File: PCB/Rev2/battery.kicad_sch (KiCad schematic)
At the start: 11 parts, among them U2 TP4057, U3 TPS2116DRL, U4 TPS2116DRL

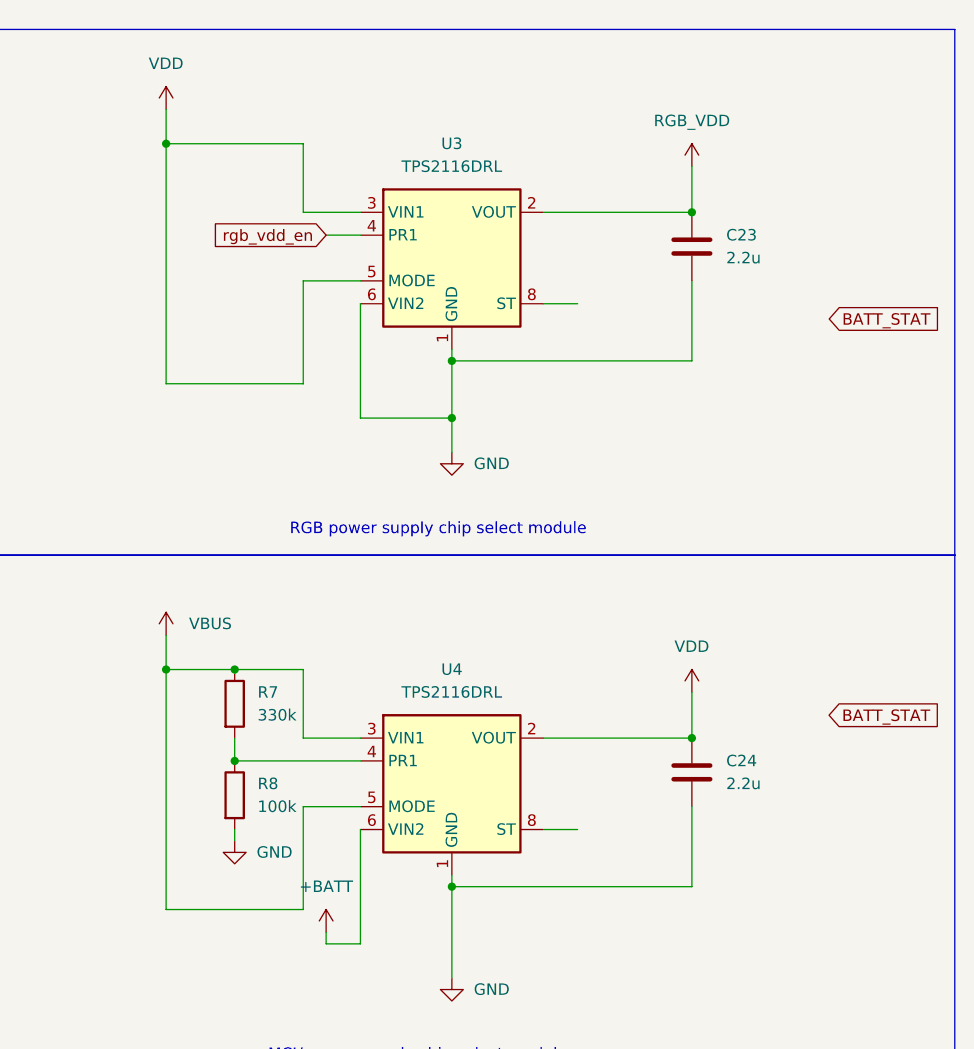
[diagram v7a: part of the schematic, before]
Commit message: Fix RGB_VDD
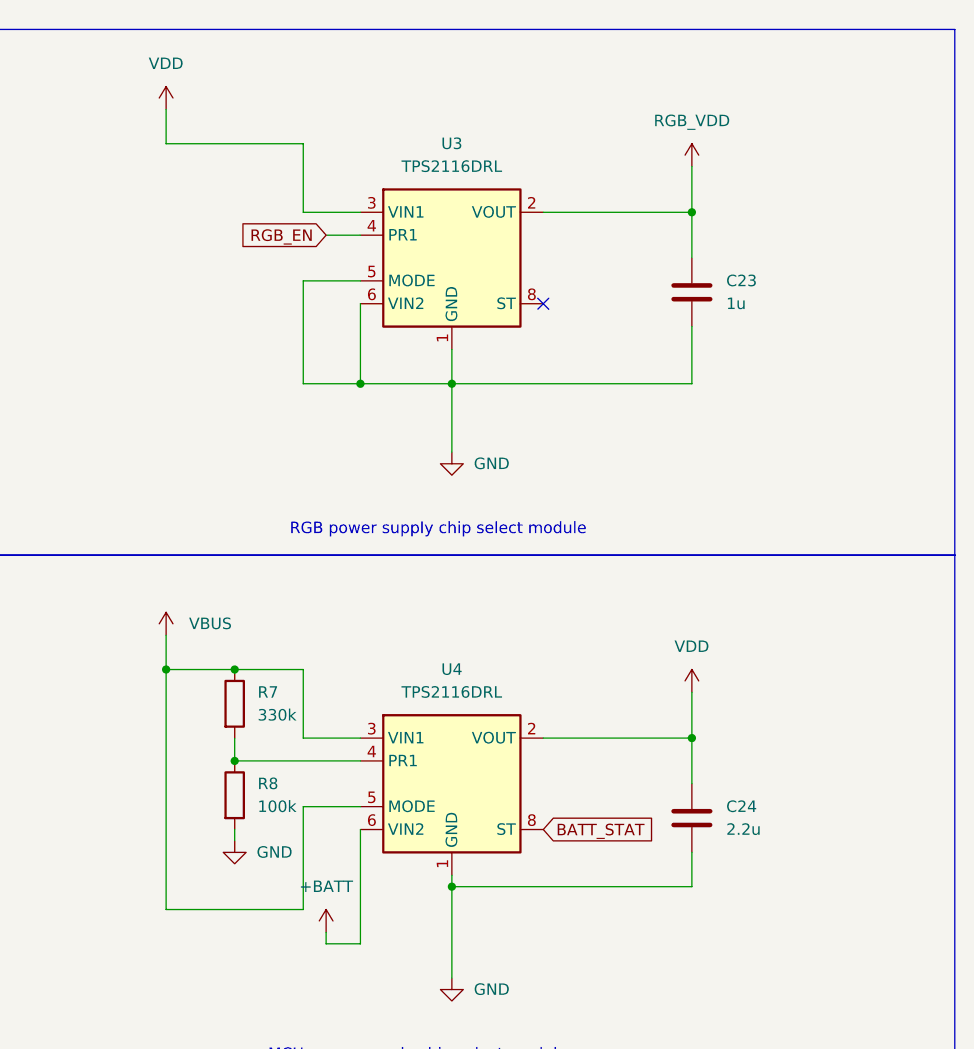
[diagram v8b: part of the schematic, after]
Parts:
- C23: value 2.2u -> 1u
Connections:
- net BATT_STAT: now also U4.8 (ST)
- net GND: now also U3.5 (MODE)
- net VDD: no longer U3.5 (MODE)
- net rgb_vdd_en renamed RGB_EN
- no-connect marks 2 -> 3
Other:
- moved on the sheet: C23
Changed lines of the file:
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@@
+	)
+	(junction
+		(at 171.45 52.07)
+		(diameter 0)
+		(color 0 0 0 0)
 	)
 	(junction
@@
 	)
 	(junction
+		(at 161.29 52.07)
+		(diameter 0)
+		(color 0 0 0 0)
+	)
+	(junction
 		(at 59.69 52.07)
 		(diameter 0)
@@
 	)
 	(junction
-		(at 171.45 55.88)
+		(at 95.25 36.83)
 		(diameter 0)
 		(color 0 0 0 0)
 	)
 	(junction
-		(at 95.25 36.83)
+		(at 198.12 91.44)
 		(diameter 0)
 		(color 0 0 0 0)
@@
 	)
 	(junction
-		(at 139.7 25.4)
-		(diameter 0)
-		(color 0 0 0 0)
-	)
-	(junction
-		(at 198.12 91.44)
-		(diameter 0)
-		(color 0 0 0 0)
-	)
-	(junction
-		(at 171.45 49.53)
-		(diameter 0)
-		(color 0 0 0 0)
-	)
-	(junction
 		(at 139.7 83.82)
 		(diameter 0)
@@
 	)
 	(no_connect
+		(at 181.61 43.18)
+	)
+	(no_connect
 		(at 49.53 46.99)
 	)
 	(wire
 		(pts
-			(xy 185.42 101.6) (xy 181.61 101.6)
+			(xy 198.12 52.07) (xy 198.12 45.72)
 		)
 		(stroke
@@
 	(wire
 		(pts
+			(xy 154.94 52.07) (xy 161.29 52.07)
+		)
+		(stroke
+			(width 0)
+			(type default)
+		)
+	)
+	(wire
+		(pts
 			(xy 171.45 107.95) (xy 198.12 107.95)
 		)
@@
 	(wire
 		(pts
-			(xy 171.45 55.88) (xy 171.45 59.69)
-		)
-		(stroke
-			(width 0)
-			(type default)
-		)
-	)
-	(wire
-		(pts
-			(xy 154.94 52.07) (xy 154.94 40.64)
-		)
-		(stroke
-			(width 0)
-			(type default)
-		)
-	)
-	(wire
-		(pts
 			(xy 139.7 110.49) (xy 154.94 110.49)
 		)
@@
 	(wire
 		(pts
-			(xy 139.7 52.07) (xy 154.94 52.07)
-		)
-		(stroke
-			(width 0)
-			(type default)
-		)
-	)
-	(wire
-		(pts
 			(xy 181.61 91.44) (xy 198.12 91.44)
 		)
@@
 	(wire
 		(pts
+			(xy 154.94 40.64) (xy 154.94 52.07)
+		)
+		(stroke
+			(width 0)
+			(type default)
+		)
+	)
+	(wire
+		(pts
 			(xy 198.12 86.36) (xy 198.12 91.44)
 		)
@@
 	(wire
 		(pts
-			(xy 171.45 49.53) (xy 171.45 55.88)
+			(xy 171.45 48.26) (xy 171.45 52.07)
+		)
+		(stroke
+			(width 0)
+			(type default)
+		)
+	)
+	(wire
+		(pts
+			(xy 171.45 52.07) (xy 171.45 59.69)
 		)
 		(stroke
@@
 	(wire
 		(pts
-			(xy 198.12 40.64) (xy 198.12 49.53)
+			(xy 171.45 52.07) (xy 198.12 52.07)
 		)
 		(stroke
@@
 	(wire
 		(pts
-			(xy 139.7 25.4) (xy 139.7 52.07)
-		)
-		(stroke
-			(width 0)
-			(type default)
-		)
-	)
-	(wire
-		(pts
-			(xy 171.45 48.26) (xy 171.45 49.53)
-		)
-		(stroke
-			(width 0)
-			(type default)
-		)
-	)
-	(wire
-		(pts
 			(xy 147.32 93.98) (xy 147.32 91.44)
 		)
@@
 	(wire
 		(pts
-			(xy 171.45 49.53) (xy 198.12 49.53)
+			(xy 198.12 104.14) (xy 198.12 107.95)
 		)
 		(stroke
@@
 	(wire
 		(pts
-			(xy 185.42 43.18) (xy 181.61 43.18)
-		)
-		(stroke
-			(width 0)
-			(type default)
-		)
-	)
-	(wire
-		(pts
 			(xy 95.25 36.83) (xy 95.25 39.37)
 		)
@@
 	(wire
 		(pts
-			(xy 198.12 99.06) (xy 198.12 107.95)
+			(xy 198.12 91.44) (xy 198.12 96.52)
+		)
+		(stroke
+			(width 0)
+			(type default)
+		)
+	)
+	(wire
+		(pts
+			(xy 198.12 38.1) (xy 198.12 33.02)
 		)
 		(stroke
@@
 	(wire
 		(pts
-			(xy 161.29 43.18) (xy 161.29 55.88)
-		)
-		(stroke
-			(width 0)
-			(type default)
-		)
-	)
-	(wire
-		(pts
-			(xy 161.29 55.88) (xy 171.45 55.88)
+			(xy 161.29 43.18) (xy 161.29 52.07)
+		)
+		(stroke
+			(width 0)
+			(type default)
+		)
+	)
+	(wire
+		(pts
+			(xy 161.29 52.07) (xy 171.45 52.07)
 		)
 		(stroke
@@
 		)
 	)
-	(global_label "rgb_vdd_en"
+	(global_label "RGB_EN"
 		(shape input)
 		(at 157.48 35.56 180)
@@
 		)
 		(property "Intersheetrefs" "${INTERSHEET_REFS}"
-			(at 143.9722 35.56 0)
+			(at 147.2377 35.56 0)
 			(effects
 				(font
@@
 	(global_label "BATT_STAT"
 		(shape input)
-		(at 213.3773 44.8722 0)
+		(at 181.61 101.6 0)
 		(fields_autoplaced yes)
 		(effects
@@
 		)
 		(property "Intersheetrefs" "${INTERSHEET_REFS}"
-			(at 225.8572 44.8722 0)
-			(effects
-				(font
-					(size 1.27 1.27)
-				)
-				(justify left)
-				(hide yes)
-			)
-		)
-	)
-	(global_label "BATT_STAT"
-		(shape input)
-		(at 213.36 88.9 0)
-		(fields_autoplaced yes)
-		(effects
-			(font
-				(size 1.27 1.27)
-			)
-			(justify left)
-		)
-		(property "Intersheetrefs" "${INTERSHEET_REFS}"
-			(at 225.8399 88.9 0)
+			(at 194.0899 101.6 0)
 			(effects
 				(font
@@
 	(symbol
 		(lib_id "Device:C")
-		(at 198.12 95.25 0)
-		(unit 1)
-		(exclude_from_sim no)
-		(in_bom yes)
-		(on_board yes)
-		(dnp no)
-		(fields_autoplaced yes)
-		(property "Reference" "C24"
-			(at 201.93 93.9799 0)
-			(effects
-				(font
-					(size 1.27 1.27)
-				)
-				(justify left)
-			)
-		)
-		(property "Value" "2.2u"
-			(at 201.93 96.5199 0)
-			(effects
-				(font
-					(size 1.27 1.27)
-				)
-				(justify left)
-			)
-		)
-		(property "Footprint" "Capacitor_SMD:C_0402_1005Metric"
-			(at 199.0852 99.06 0)
-			(effects
-				(font
-					(size 1.27 1.27)
-				)
-				(hide yes)
-			)
-		)
-		(property "Datasheet" "~"
-			(at 198.12 95.25 0)
-			(effects
-				(font
-					(size 1.27 1.27)
-				)
-				(hide yes)
-			)
-		)
-		(property "Description" "Unpolarized capacitor"
-			(at 198.12 95.25 0)
-			(effects
-				(font
-					(size 1.27 1.27)
-				)
-				(hide yes)
-			)
-		)
-		(pin "2"
-		)
-		(pin "1"
-		)
-		(instances
-			(project "PH60-SC_Rev2"
-				(path "/dca0f898-8fdb-4522-a51d-f4f4238906e7/65afedf5-5b27-4d53-9ad9-9264a927261c"
-					(reference "C24")
-					(unit 1)
-				)
-			)
-		)
-	)
-	(symbol
-		(lib_id "Device:C")
-		(at 198.12 36.83 0)
+		(at 198.12 41.91 0)
 		(unit 1)
 		(exclude_from_sim no)
@@
 		(fields_autoplaced yes)
 		(property "Reference" "C23"
-			(at 201.93 35.5599 0)
-			(effects
-				(font
-					(size 1.27 1.27)
-				)
-				(justify left)
-			)
-		)
-		(property "Value" "2.2u"
-			(at 201.93 38.0999 0)
+			(at 201.93 40.6399 0)
+			(effects
+				(font
+					(size 1.27 1.27)
+				)
+				(justify left)
+			)
+		)
+		(property "Value" "1u"
+			(at 201.93 43.1799 0)
 			(effects
 				(font
@@
 		)
 		(property "Footprint" "Capacitor_SMD:C_0402_1005Metric"
-			(at 199.0852 40.64 0)
+			(at 199.0852 45.72 0)
 			(effects
 				(font
@@
 		)
 		(property "Datasheet" "~"
-			(at 198.12 36.83 0)
+			(at 198.12 41.91 0)
 			(effects
 				(font
@@
 		)
 		(property "Description" "Unpolarized capacitor"
-			(at 198.12 36.83 0)
+			(at 198.12 41.91 0)
 			(effects
 				(font
@@
 					(unit 1)
 				)
+			)
+		)
+	)
+	(symbol
+		(lib_id "Device:C")
+		(at 198.12 100.33 0)
+		(unit 1)
+		(exclude_from_sim no)
+		(in_bom yes)
+		(on_board yes)
+		(dnp no)
+		(fields_autoplaced yes)
+		(property "Reference" "C24"
+			(at 201.93 99.0599 0)
+			(effects
+				(font
+					(size 1.27 1.27)
+				)
+				(justify left)
+			)
+		)
+		(property "Value" "2.2u"
+			(at 201.93 101.5999 0)
+			(effects
+				(font
+					(size 1.27 1.27)
+				)
+				(justify left)
+			)
+		)
+		(property "Footprint" "Capacitor_SMD:C_0402_1005Metric"
+			(at 199.0852 104.14 0)
+			(effects
+				(font
+					(size 1.27 1.27)
+				)
+				(hide yes)
+			)
+		)
+		(property "Datasheet" "~"
+			(at 198.12 100.33 0)
+			(effects
+				(font
+					(size 1.27 1.27)
+				)
+				(hide yes)
+			)
+		)
+		(property "Description" "Unpolarized capacitor"
+			(at 198.12 100.33 0)
+			(effects
+				(font
+					(size 1.27 1.27)
+				)
+				(hide yes)
+			)
+		)
+		(pin "2"
+		)
+		(pin "1"
+		)
+		(instances
+			(project "PH60-SC_Rev2"
+				(path "/dca0f898-8fdb-4522-a51d-f4f4238906e7/65afedf5-5b27-4d53-9ad9-9264a927261c"
+					(reference "C24")
+					(unit 1)
+				)
